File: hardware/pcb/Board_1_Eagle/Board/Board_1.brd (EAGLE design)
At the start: 160 x 100 mm, 88 parts, among them IC1 MCP73831, IC2 LT1963EST-1.5, IC3 VUB300, IC4 TS3A27, IC5 WTV020SD-20S, J3 DEBUG_CONNECTOR, SW1 SW_TACT_SMD, SW2 SW_TACT_SMD, SW3 SW_TACT_SMD, SW4 SW_TACT_SMD, SW5 SW_TACT_SMD, SW6 SW_TACT_SMD, SW7 SW_TACT_SMD, X1 1751248, X2 1751248, X3 1751248, Y1 CRYSTAL.3.2X2.5MM

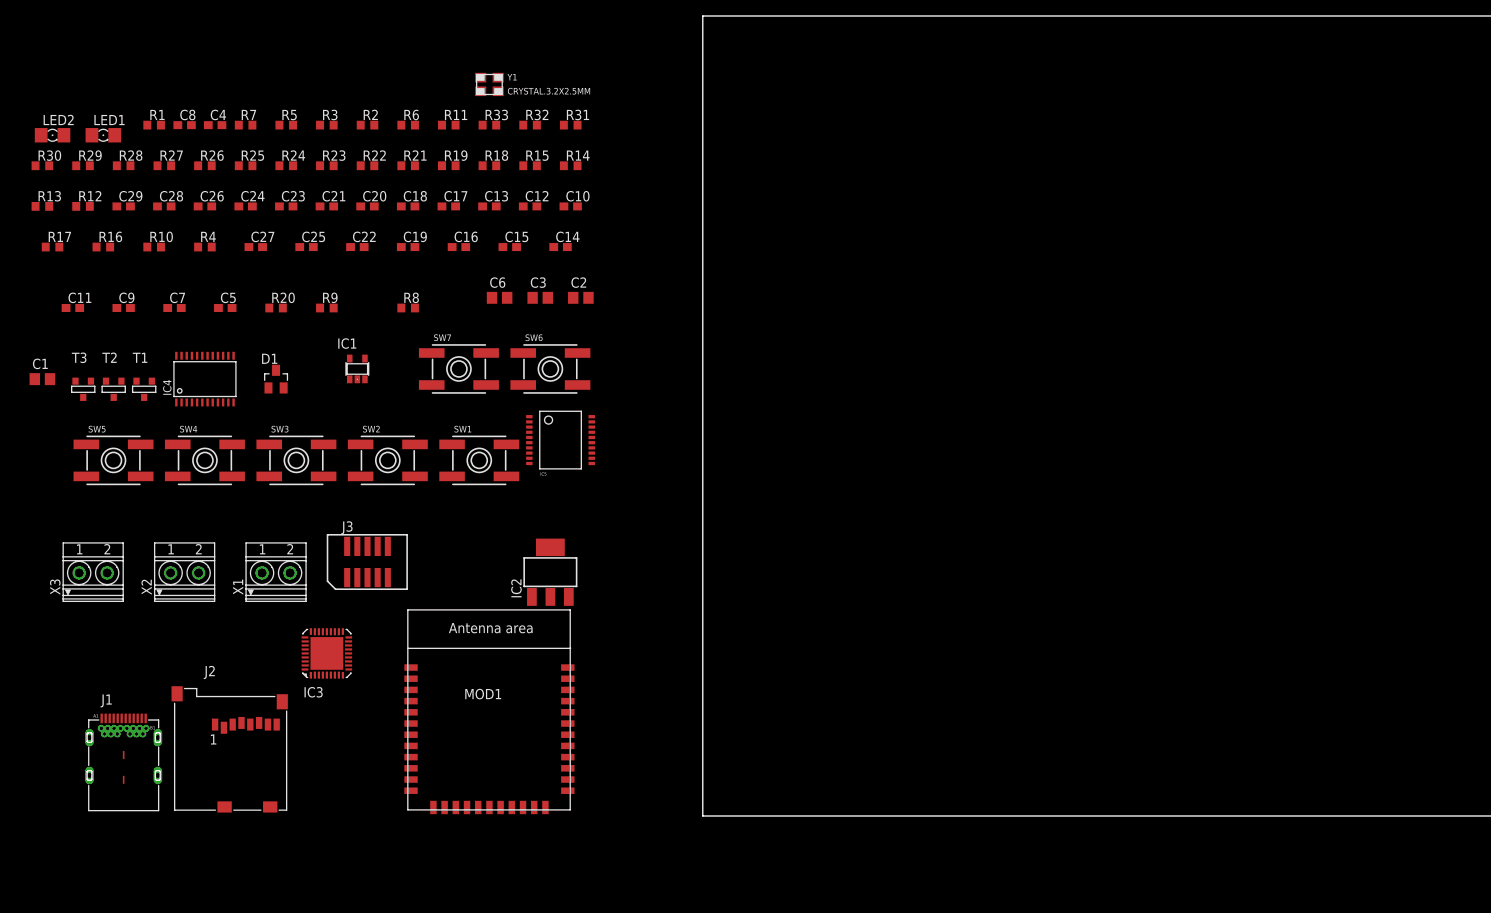
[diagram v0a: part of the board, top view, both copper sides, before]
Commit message: First part of layout done and added design rules.
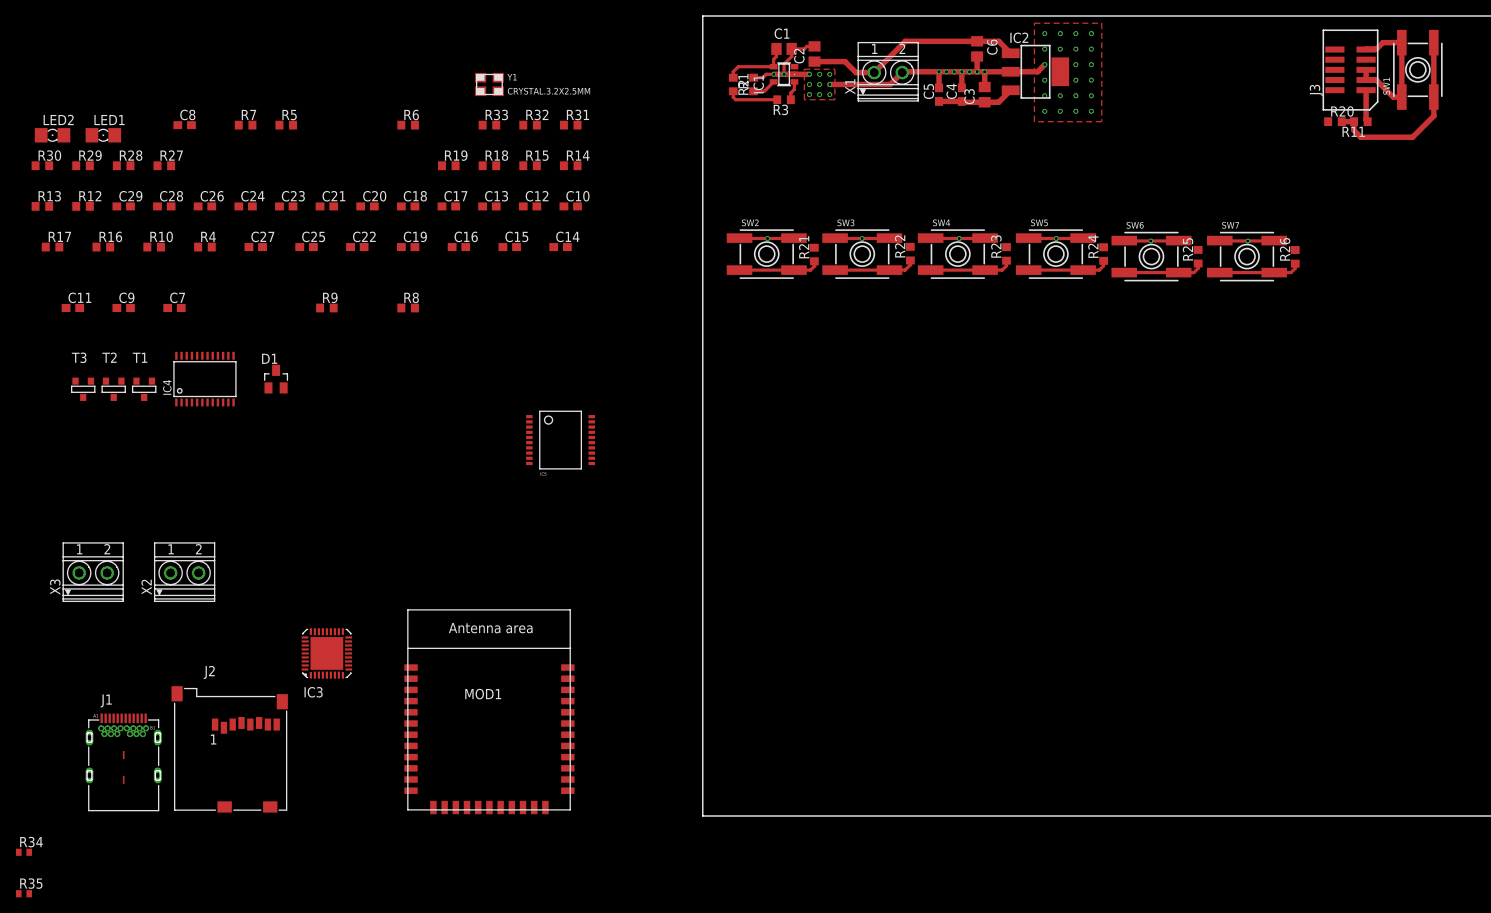
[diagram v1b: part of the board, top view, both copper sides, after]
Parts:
- added R34, R35: 15k, resistor:R0402
- moved J3 137.4 mm to (81.0, 93.3), turned to 90 degrees
- moved R26 136.8 mm to (74.1, 69.9), turned to 90 degrees
- moved R20 134.4 mm to (79.0, 86.8)
- moved SW1 127.1 mm to (89.4, 93.3), turned to 90 degrees
- moved SW5 120.6 mm to (44.1, 70.2)
- moved R25 119.6 mm to (61.9, 69.9), turned to 90 degrees
- moved R11 114.0 mm to (82.3, 86.8), turned to 180 degrees
- moved R24 102.8 mm to (50.1, 70.2), turned to 90 degrees
- moved C1 101.5 mm to (10.2, 95.9)
- moved SW7 99.5 mm to (68.0, 69.9)
- moved X1 98.8 mm to (23.2, 93.0)
- moved SW4 97.6 mm to (31.9, 70.2)
- moved C4 93.4 mm to (32.4, 90.2), turned to 90 degrees
- moved C5 93.1 mm to (29.5, 90.2), turned to 90 degrees
- moved IC2 87.1 mm to (41.6, 93.0), turned to 270 degrees
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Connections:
- removed net N$51: R31.2
- net +3V3: now also R34.1, R35.1
- net D+: now also R35.2
- net D-: now also R34.2
- net V+: now also R31.2
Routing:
- net GND: track 0.00 -> 110.1 mm, vias 0 -> 46
- net V+: track 0.00 -> 27.3 mm
- net N$48: track 0.00 -> 23.2 mm
- net +3V3: track 0.00 -> 13.6 mm
- net TASTE2: track 0.00 -> 10.3 mm
- net TASTE5: track 0.00 -> 10.2 mm
- net TASTE1: track 0.00 -> 10.2 mm
- net TASTE0: track 0.00 -> 10.2 mm
- net TASTE3: track 0.00 -> 10.2 mm
- net TASTE4: track 0.00 -> 10.1 mm
- net +5V: track 0.00 -> 8.42 mm
- net N$2: track 0.00 -> 6.37 mm
- net N$1: track 0.00 -> 2.99 mm
- net N$3: track 0.00 -> 2.41 mm
- added copper zone on layer 1, net GND

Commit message: VUB300 gelayoutet
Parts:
- C10, C11, C12, C13, C14, C15, C16, C17, C18, C19, C20, C21, C7, C8, C9: device rcl:C0603 -> rcl:C0402
- R12, R13, R14, R15, R4, R5, R6, R7: device resistor:R0603 -> resistor:R0402
- moved C11 370.0 mm to (291.1, 72.6), flipped to the bottom, turned to 180 degrees
- moved C9 367.8 mm to (295.3, 73.2), flipped to the bottom
- moved C7 361.1 mm to (295.0, 69.5), flipped to the bottom, turned to 90 degrees
- moved C8 358.3 mm to (293.2, 70.8), flipped to the bottom, turned to 90 degrees
- moved R4 357.6 mm to (295.4, 67.7)
- moved R7 349.7 mm to (292.5, 78.5)
- moved R5 348.5 mm to (296.3, 77.5), turned to 90 degrees
- moved IC3 340.5 mm to (292.8, 72.9), turned to 270 degrees
- moved C21 337.9 mm to (290.9, 79.6), turned to 180 degrees
- moved C20 335.9 mm to (294.0, 79.6), turned to 180 degrees
- moved R6 327.7 mm to (290.8, 78.1), flipped to the bottom, turned to 90 degrees
- moved C19 326.3 mm to (289.4, 78.4), turned to 180 degrees
- moved C18 326.2 mm to (289.4, 77.3), turned to 180 degrees
- moved C17 323.5 mm to (291.7, 75.5), flipped to the bottom, turned to 180 degrees
- moved C16 322.2 mm to (291.7, 74.4), flipped to the bottom, turned to 180 degrees
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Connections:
- net D+ renamed D_P
- net D- renamed D_N
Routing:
- net +3V3: track 13.6 -> 151.3 mm, vias 0 -> 12
- net N$52: track 0.00 -> 39.8 mm
- net TASTE0: track 10.2 -> 48.7 mm
- net TASTE5: track 10.2 -> 40.7 mm
- net TASTE2: track 10.3 -> 38.9 mm
- net WP: track 0.00 -> 24.7 mm
- net TASTE4: track 10.1 -> 29.9 mm
- net NCD: track 0.00 -> 19.1 mm
- net TASTE1: track 10.2 -> 29.1 mm
- net D2: track 0.00 -> 18.5 mm
- net D3: track 0.00 -> 18.3 mm
- net TASTE3: track 10.2 -> 25.6 mm
- net N$53: track 0.00 -> 14.1 mm
- net N$50: track 0.00 -> 14.1 mm
- net D1: track 0.00 -> 12.0 mm
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- added copper zone on layer 1, net +5V
- added copper zone on layer 16, net GND
- added copper zone on layer 1, net V+
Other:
- board text added: "S1"
- board text added: "S2"
- board text added: "S3"
- board text added: "S4"
- board text added: "S5"
- board text added: "S6"
